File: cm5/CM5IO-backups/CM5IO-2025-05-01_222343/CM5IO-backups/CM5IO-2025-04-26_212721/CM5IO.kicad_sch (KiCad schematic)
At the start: 11 parts, among them J2 B2B-XH-A_LF__SN_

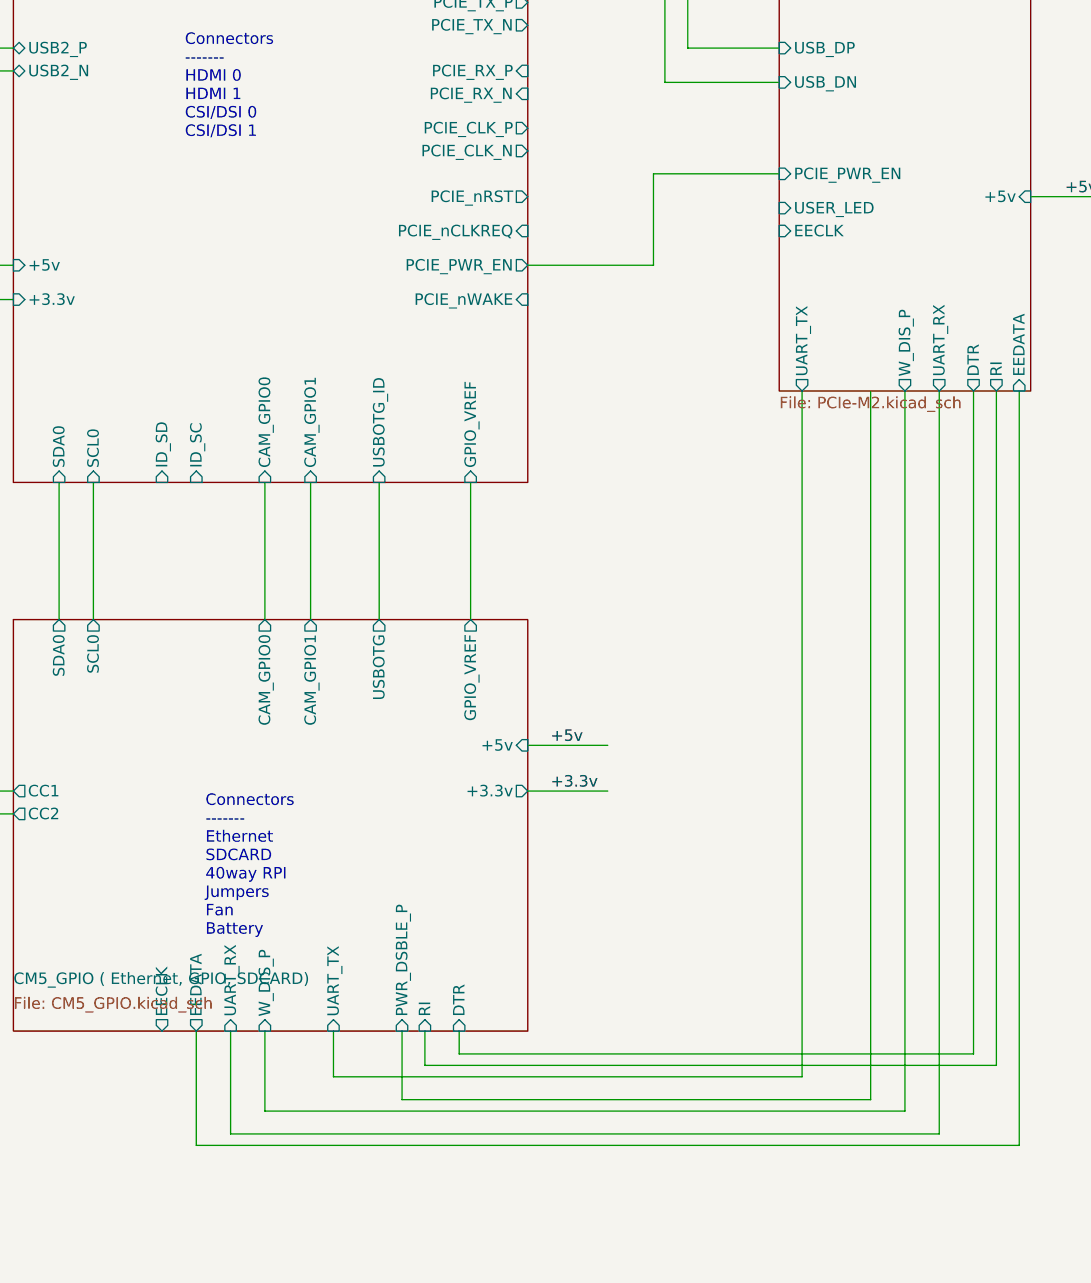
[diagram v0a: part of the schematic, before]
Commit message: Delete some unnecessary components and fix up some of the trace thicknesses
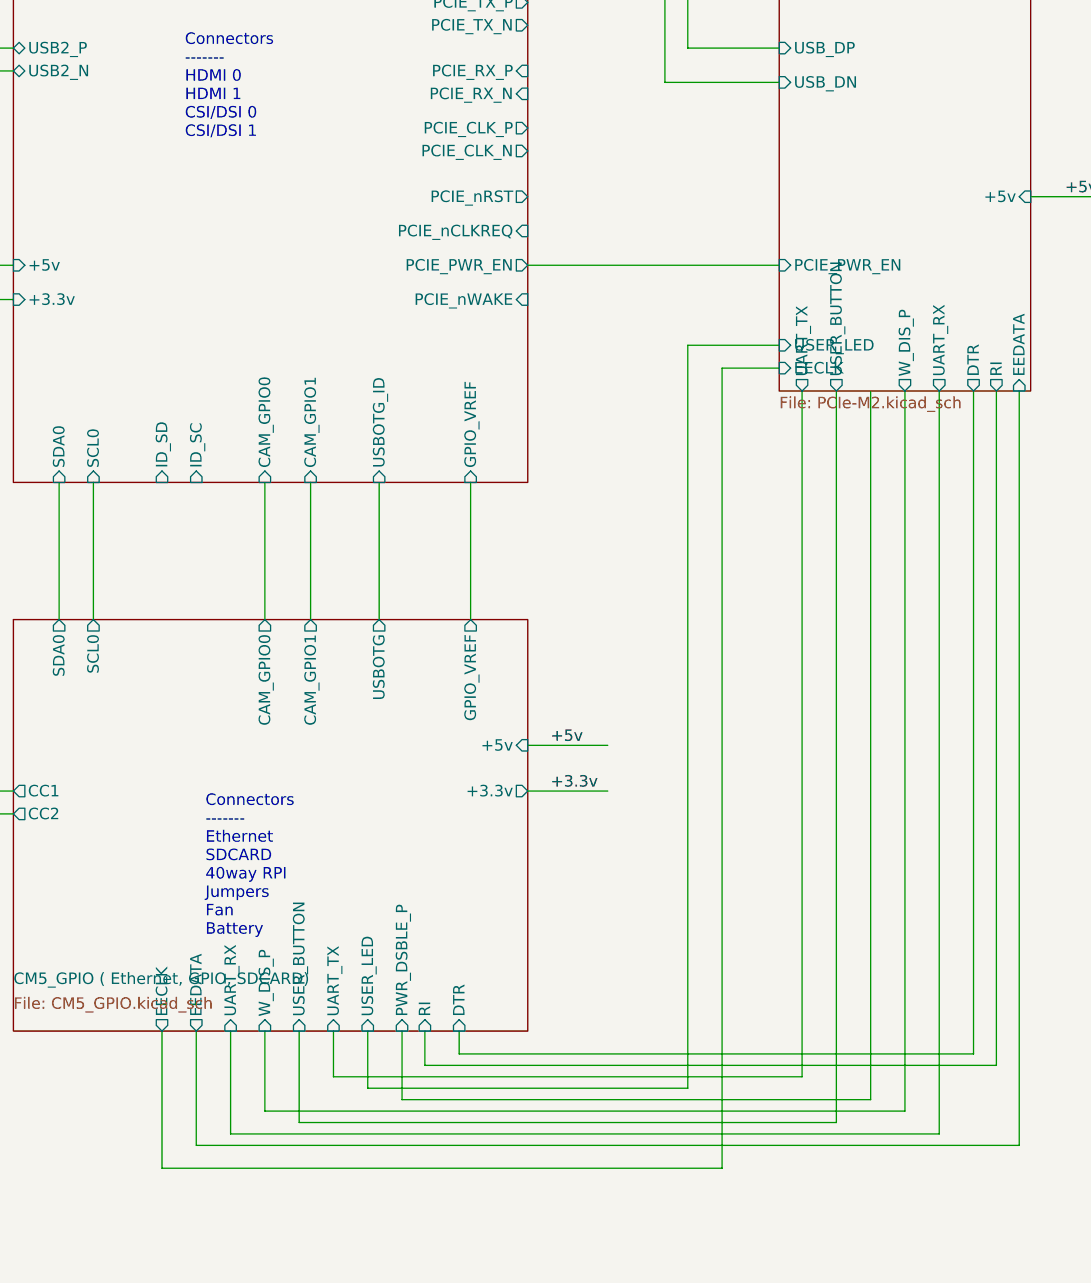
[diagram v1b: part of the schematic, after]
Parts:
- C18, C9: LCSC C327024 -> (none)
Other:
- sheet CM5_GPIO ( Ethernet, GPIO, SDCARD) ports: added USER_BUTTON, USER_LED; removed none
- sheet PCIe-M2 ports: added USER_BUTTON; removed none
- company: Ridgeline Radio -> E-SMART SOLUTIONS
- title: Alas Compute Module 5 IO -> Compute Module 5 IO
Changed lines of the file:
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@@
 	(paper "A4")
 	(title_block
-		(title "Alas Compute Module 5 IO")
+		(title "Compute Module 5 IO")
 		(rev "1")
-		(company "Ridgeline Radio")
-		(comment 1 "Jake Wood")
+		(company "E-SMART SOLUTIONS")
+		(comment 1 "Mostafa Bkair")
 	)
 	(text "Connectors\n-------\nEthernet\nSDCARD\n40way RPI\nJumpers\nFan\nBattery"
@@
 	(wire
 		(pts
+			(xy 186.69 72.39) (xy 214.63 72.39)
+		)
+		(stroke
+			(width 0)
+			(type default)
+		)
+	)
+	(wire
+		(pts
 			(xy 180.34 96.52) (xy 180.34 111.76)
 		)
@@
 	(wire
 		(pts
-			(xy 186.69 72.39) (xy 200.66 72.39)
+			(xy 146.05 172.72) (xy 146.05 157.48)
 		)
 		(stroke
@@
 	(wire
 		(pts
+			(xy 208.28 83.82) (xy 208.28 172.72)
+		)
+		(stroke
+			(width 0)
+			(type default)
+		)
+	)
+	(wire
+		(pts
+			(xy 208.28 172.72) (xy 146.05 172.72)
+		)
+		(stroke
+			(width 0)
+			(type default)
+		)
+	)
+	(wire
+		(pts
 			(xy 204.47 48.26) (xy 214.63 48.26)
 		)
@@
 	(wire
 		(pts
-			(xy 200.66 62.23) (xy 214.63 62.23)
-		)
-		(stroke
-			(width 0)
-			(type default)
-		)
-	)
-	(wire
-		(pts
 			(xy 92.71 101.6) (xy 104.14 101.6)
 		)
@@
 	(wire
 		(pts
+			(xy 204.47 81.28) (xy 204.47 163.83)
+		)
+		(stroke
+			(width 0)
+			(type default)
+		)
+	)
+	(wire
+		(pts
 			(xy 149.86 170.18) (xy 241.3 170.18)
 		)
@@
 	(wire
 		(pts
+			(xy 214.63 81.28) (xy 204.47 81.28)
+		)
+		(stroke
+			(width 0)
+			(type default)
+		)
+	)
+	(wire
+		(pts
 			(xy 162.56 96.52) (xy 162.56 111.76)
 		)
@@
 	(wire
 		(pts
-			(xy 200.66 72.39) (xy 200.66 62.23)
-		)
-		(stroke
-			(width 0)
-			(type default)
-		)
-	)
-	(wire
-		(pts
 			(xy 129.54 50.8) (xy 120.65 50.8)
 		)
@@
 	(wire
 		(pts
+			(xy 161.29 157.48) (xy 161.29 167.64)
+		)
+		(stroke
+			(width 0)
+			(type default)
+		)
+	)
+	(wire
+		(pts
 			(xy 242.57 64.77) (xy 255.27 64.77)
 		)
@@
 	(wire
 		(pts
+			(xy 214.63 83.82) (xy 208.28 83.82)
+		)
+		(stroke
+			(width 0)
+			(type default)
+		)
+	)
+	(wire
+		(pts
 			(xy 232.41 86.36) (xy 232.41 168.91)
 		)
@@
 	(wire
 		(pts
+			(xy 168.91 163.83) (xy 204.47 163.83)
+		)
+		(stroke
+			(width 0)
+			(type default)
+		)
+	)
+	(wire
+		(pts
 			(xy 186.69 125.73) (xy 195.58 125.73)
 		)
@@
 	(wire
 		(pts
+			(xy 168.91 163.83) (xy 168.91 157.48)
+		)
+		(stroke
+			(width 0)
+			(type default)
+		)
+	)
+	(wire
+		(pts
 			(xy 120.65 20.32) (xy 201.93 20.32)
 		)
@@
 	(wire
 		(pts
+			(xy 161.29 167.64) (xy 220.98 167.64)
+		)
+		(stroke
+			(width 0)
+			(type default)
+		)
+	)
+	(wire
+		(pts
 			(xy 123.19 22.86) (xy 204.47 22.86)
 		)
@@
 		(pts
 			(xy 238.76 161.29) (xy 175.26 161.29)
+		)
+		(stroke
+			(width 0)
+			(type default)
+		)
+	)
+	(wire
+		(pts
+			(xy 220.98 167.64) (xy 220.98 86.36)
 		)
 		(stroke
@@
 		)
 		(property "Part Description" "	0.1uF 10% 16V Ceramic Capacitor X7R 0402 (1005 Metric)"
-			(at 104.14 97.79 0)
-			(effects
-				(font
-					(size 1.27 1.27)
-				)
-				(hide yes)
-			)
-		)
-		(property "LCSC" "C327024"
 			(at 104.14 97.79 0)
 			(effects
@@
 			)
 		)
-		(property "LCSC" "C327024"
-			(at 92.71 97.79 0)
-			(effects
-				(font
-					(size 1.27 1.27)
-				)
-				(hide yes)
-			)
-		)
 		(pin "1"
 		)
@@
 			)
 		)
+		(pin "USER_LED" input
+			(at 168.91 157.48 270)
+			(effects
+				(font
+					(size 1.27 1.27)
+				)
+				(justify left)
+			)
+		)
 		(pin "UART_TX" input
 			(at 165.1 157.48 270)
+			(effects
+				(font
+					(size 1.27 1.27)
+				)
+				(justify left)
+			)
+		)
+		(pin "USER_BUTTON" input
+			(at 161.29 157.48 270)
 			(effects
 				(font
@@
 		)
 		(pin "PCIE_PWR_EN" input
-			(at 214.63 62.23 180)
+			(at 214.63 72.39 180)
 			(effects
 				(font
@@
 			)
 		)
+		(pin "USER_BUTTON" output
+			(at 220.98 86.36 270)
+			(effects
+				(font
+					(size 1.27 1.27)
+				)
+				(justify left)
+			)
+		)
 		(pin "W_DIS_P" output
 			(at 228.6 86.36 270)
@@
 		)
 		(pin "EECLK" input
-			(at 214.63 68.58 180)
+			(at 214.63 83.82 180)
 			(effects
 				(font
@@
 		)
 		(pin "USER_LED" input
-			(at 214.63 66.04 180)
-			(effects
-				(font
+			(at 214.63 81.28 180)
+			(effects
+				(font
